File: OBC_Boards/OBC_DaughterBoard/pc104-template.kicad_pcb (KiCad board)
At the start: 4 copper layers, 90.2 x 95.9 mm, 58 parts, among them J1 PC104_Connector, J2 ST11S008V4HR2000, J3 Raspberry Pi 4 Connector, J4 3.3V Input (Testing), J5 5V Input (Testing), J6 Test Connector, J7 Temp Sens1 Connector, J8 Temp Sens2 Connector, Q1 Q_PMOS_DGS, U1 MCP9808T-E/MC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

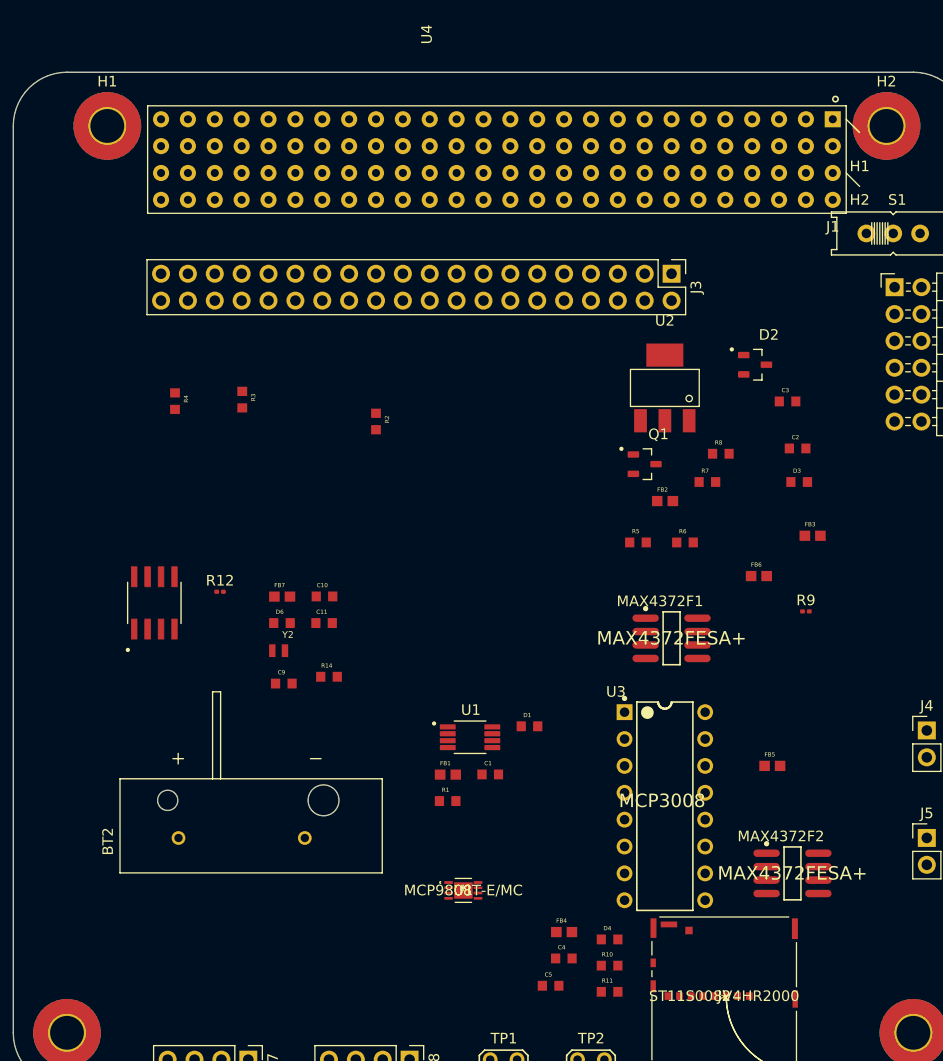
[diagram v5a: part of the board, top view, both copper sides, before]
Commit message: Adding power and group planes
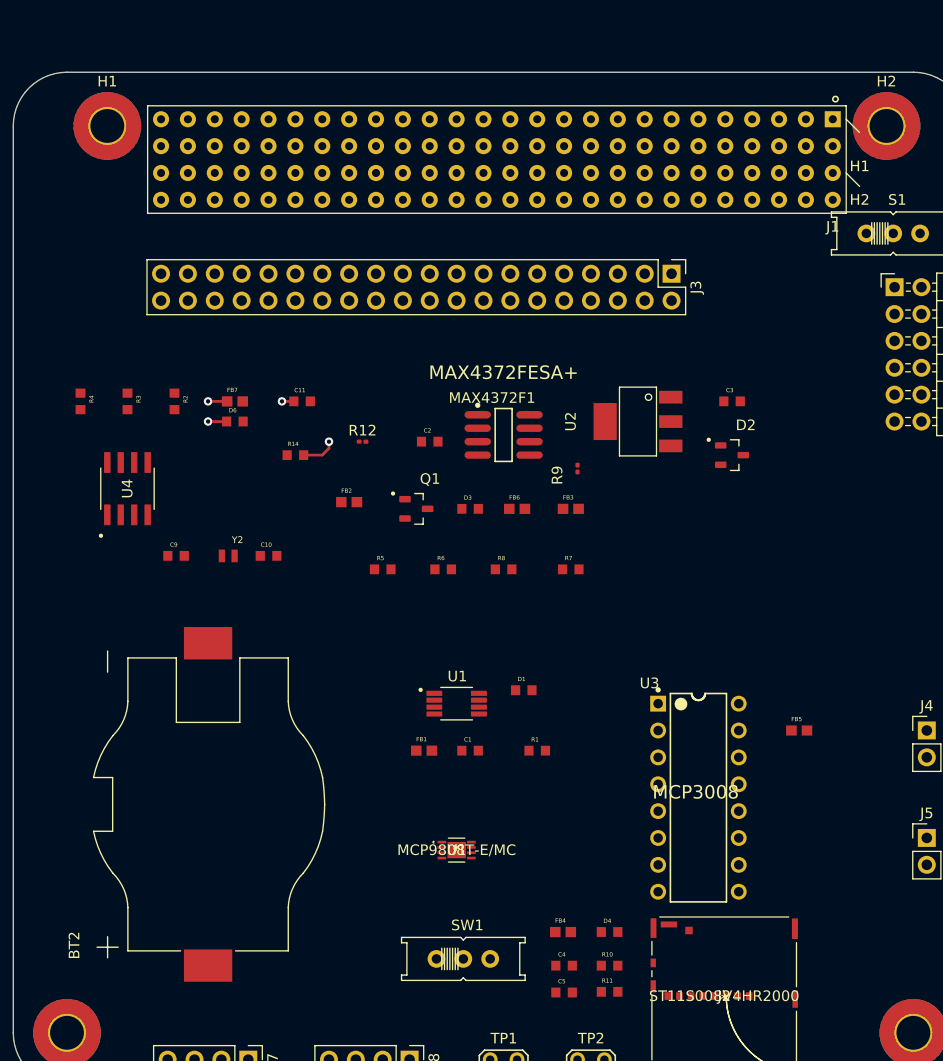
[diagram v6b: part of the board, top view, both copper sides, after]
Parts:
- removed MAX4372F2: MAX4372FESA+, Daughterboard_footprints:Maxim-MAX4372FESA+-Level_A
- added SW1: SW_DIP_x01, Daughterboard_footprints:EG1218, F.Cu at (151.8, 130.8)
- BT2: value BVSD-2032-PC -> BHSD-2032-SM; footprint Daughterboard_footprints:BAT_BVSD-2032-PC -> Daughterboard_footprints:BAT_BHSD-2032-SM
- R2, R3, R4: footprint ESR03EZPF1002:RESC1608X55N -> Daughterboard_footprints:RESC1608X55N
- moved C2 34.8 mm to (148.6, 81.9)
- moved D3 31.2 mm to (152.4, 88.3)
- moved FB2 29.9 mm to (141.0, 87.6)
- moved R9 25.5 mm to (162.6, 84.5), turned to 90 degrees
- moved MAX4372F1 24.9 mm to (155.6, 81.3)
- moved R5 24.3 mm to (144.1, 94.0)
- moved FB6 23.7 mm to (156.8, 88.3)
- moved R8 23.3 mm to (155.6, 94.0)
- moved FB3 23.0 mm to (161.9, 88.3)
- moved R6 23.0 mm to (149.9, 94.0)
- moved Q1 22.0 mm to (147.3, 88.3)
- moved R14 21.2 mm to (135.9, 83.2)
- moved C11 21.1 mm to (136.5, 78.1)
- moved R12 19.6 mm to (142.2, 81.9)
- moved D6 19.6 mm to (130.2, 80.0)
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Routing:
- net GND: track 0.00 -> 4.42 mm, vias 0 -> 2
- net +3.3V: track 0.00 -> 3.56 mm, vias 0 -> 2
- added copper zone on In2.Cu, net +3V3
- added copper zone on In1.Cu, net GND

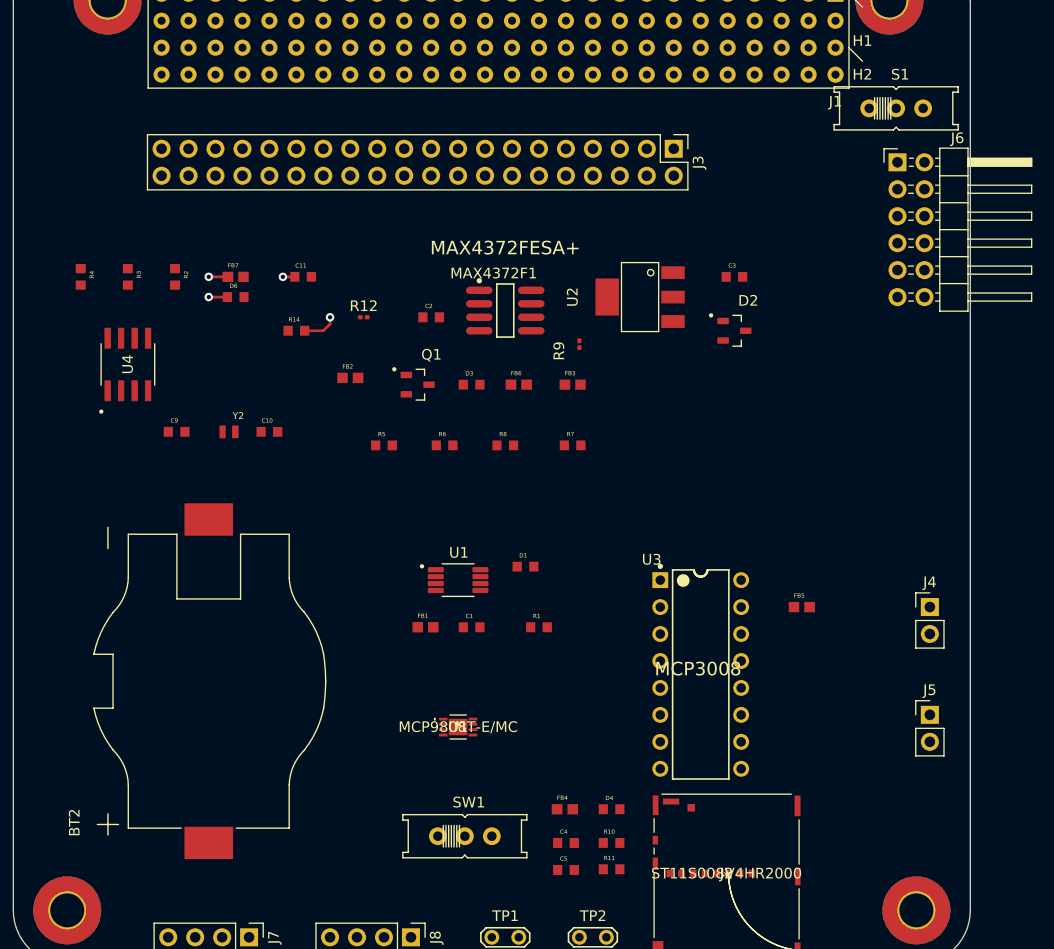
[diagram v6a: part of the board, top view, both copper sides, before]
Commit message: adding charging circuit
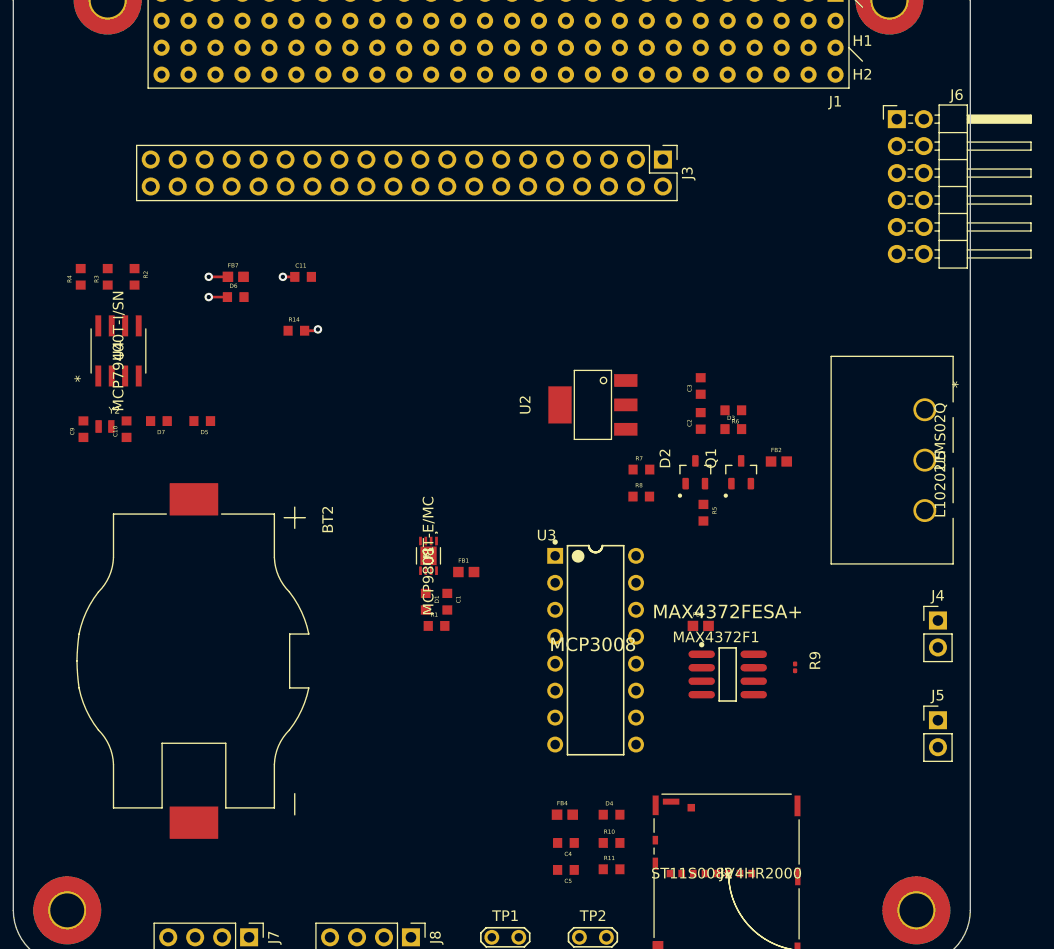
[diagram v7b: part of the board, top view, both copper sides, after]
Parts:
- removed FB3, FB5: 100R @ 100 MHz, Daughterboard_footprints:BEADC1608X75N
- removed R12: 100m, Resistor_SMD:R_0201_0603Metric
- removed S1: EG1218, Daughterboard_footprints:EG1218
- removed SW1: SW_DIP_x01, Daughterboard_footprints:EG1218
- removed the U1 at (151.1, 106.7)
- added D5: DIODE, Daughterboard_footprints:CAPC1608X90N, F.Cu at (127.0, 91.7)
- added D7: DIODE, Daughterboard_footprints:CAPC1608X90N, F.Cu at (122.9, 91.7)
- added U5: L102021MS02Q, Daughterboard_footprints:L102021MS02Q, F.Cu at (195.1, 90.6)
- U4: footprint Daughterboard_footprints:SOIC127P600X175-8N -> Daughterboard_footprints:MCP79400T-I&slash_SN
- moved FB2 41.1 mm to (181.4, 95.5)
- moved MAX4372F1 40.2 mm to (176.5, 115.6)
- moved R9 36.6 mm to (182.9, 114.9), turned to -90 degrees
- moved Q1 31.6 mm to (177.8, 96.5), turned to 90 degrees
- moved R5 30.8 mm to (174.2, 100.3), turned to -90 degrees
- moved FB6 28.5 mm to (174.0, 111.0)
- moved R6 27.4 mm to (177.1, 90.7), turned to 180 degrees
- moved C2 27.2 mm to (174.0, 91.7), turned to 90 degrees
- moved D3 25.0 mm to (177.1, 92.5)
- moved U1 16.4 mm to (148.3, 104.4), turned to -90 degrees
- moved D2 13.8 mm to (173.5, 96.5), turned to 90 degrees
- moved R8 13.7 mm to (168.4, 98.8)
- moved C10 13.5 mm to (119.9, 92.5), turned to 90 degrees
- moved Y2 11.7 mm to (117.9, 92.2)
- moved U2 11.1 mm to (163.8, 90.2)
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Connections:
- BT2 pad +: VCC_BAT -> Net-(BT2-Pad+)
- U4 pad 7: unconnected-(U4-Pad7) -> RTC_MFP
- U4 pad 8: unconnected-(U4-Pad8) -> Net-(C11-Pad2)
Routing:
- net GND: track 4.42 -> 2.43 mm

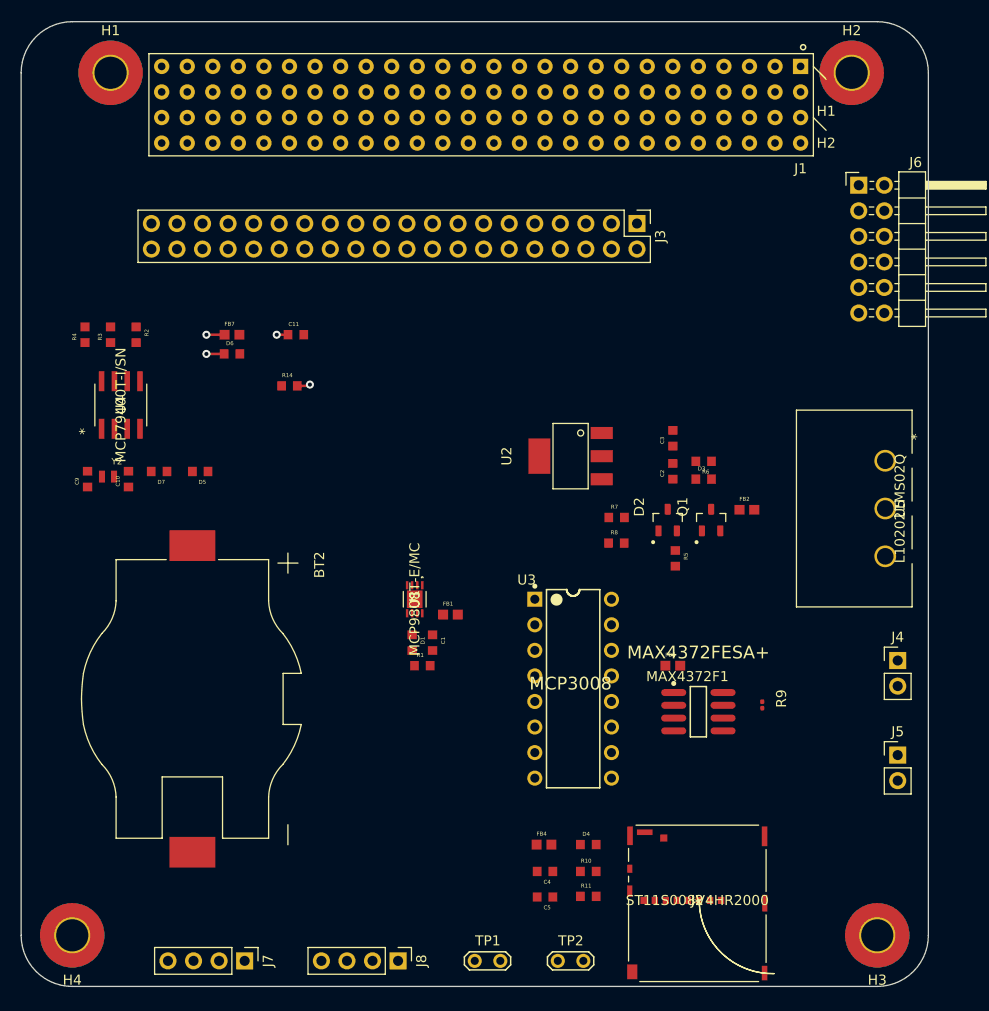
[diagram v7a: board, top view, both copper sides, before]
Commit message: adding cutouts
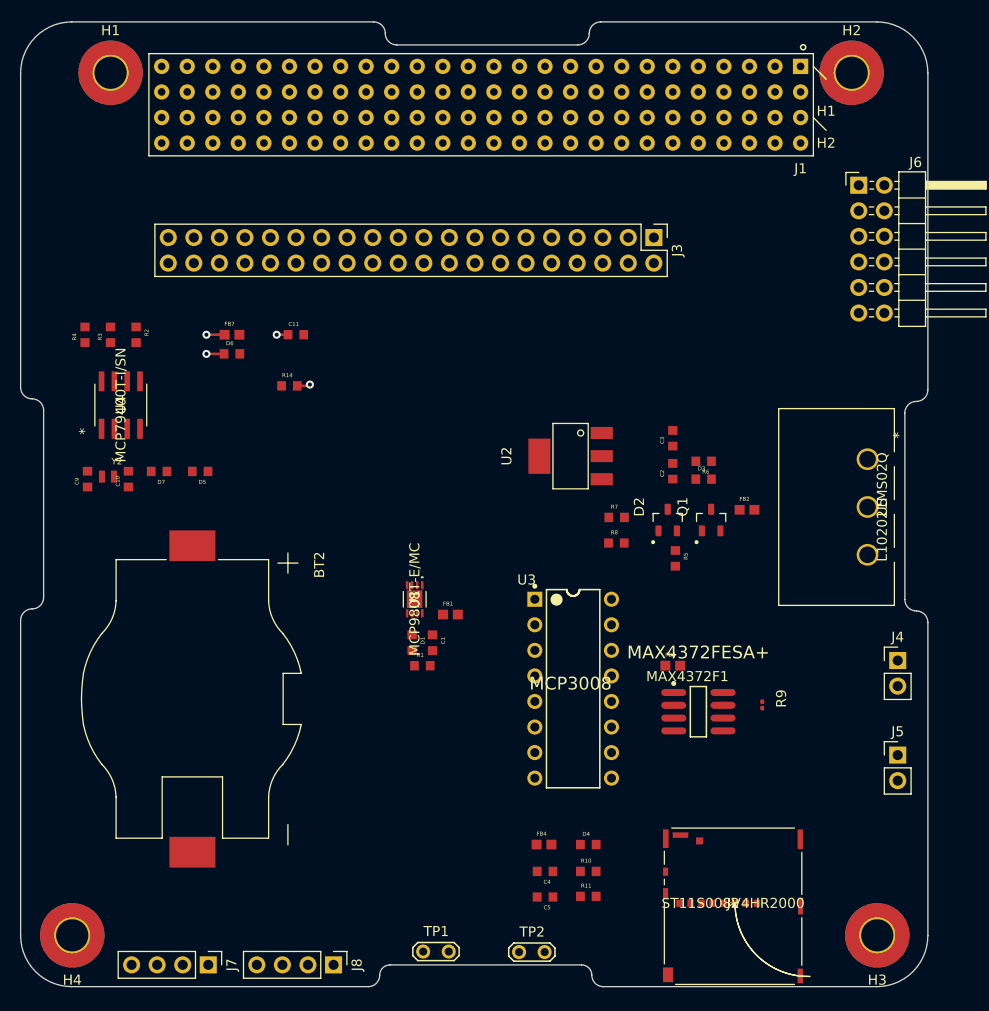
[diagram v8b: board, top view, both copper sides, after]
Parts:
- moved J8 6.43 mm to (140.3, 140.7)
- moved TP1 5.21 mm to (149.2, 139.4)
- moved TP2 3.95 mm to (158.7, 139.5)
- moved J7 3.64 mm to (127.8, 140.7)
- moved J2 3.57 mm to (180.0, 134.9)
- moved J3 2.18 mm to (172.1, 68.4)
- moved U5 1.77 mm to (193.3, 90.5)
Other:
- outline, holes or cut-outs redrawn
